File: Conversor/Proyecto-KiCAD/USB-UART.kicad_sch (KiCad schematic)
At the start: 30 parts, among them P12 USB-B, Q5 IRF7425, SW5 Switch, U14 FT232BL, U15 LP2985-3.3, Y1 6 MHz

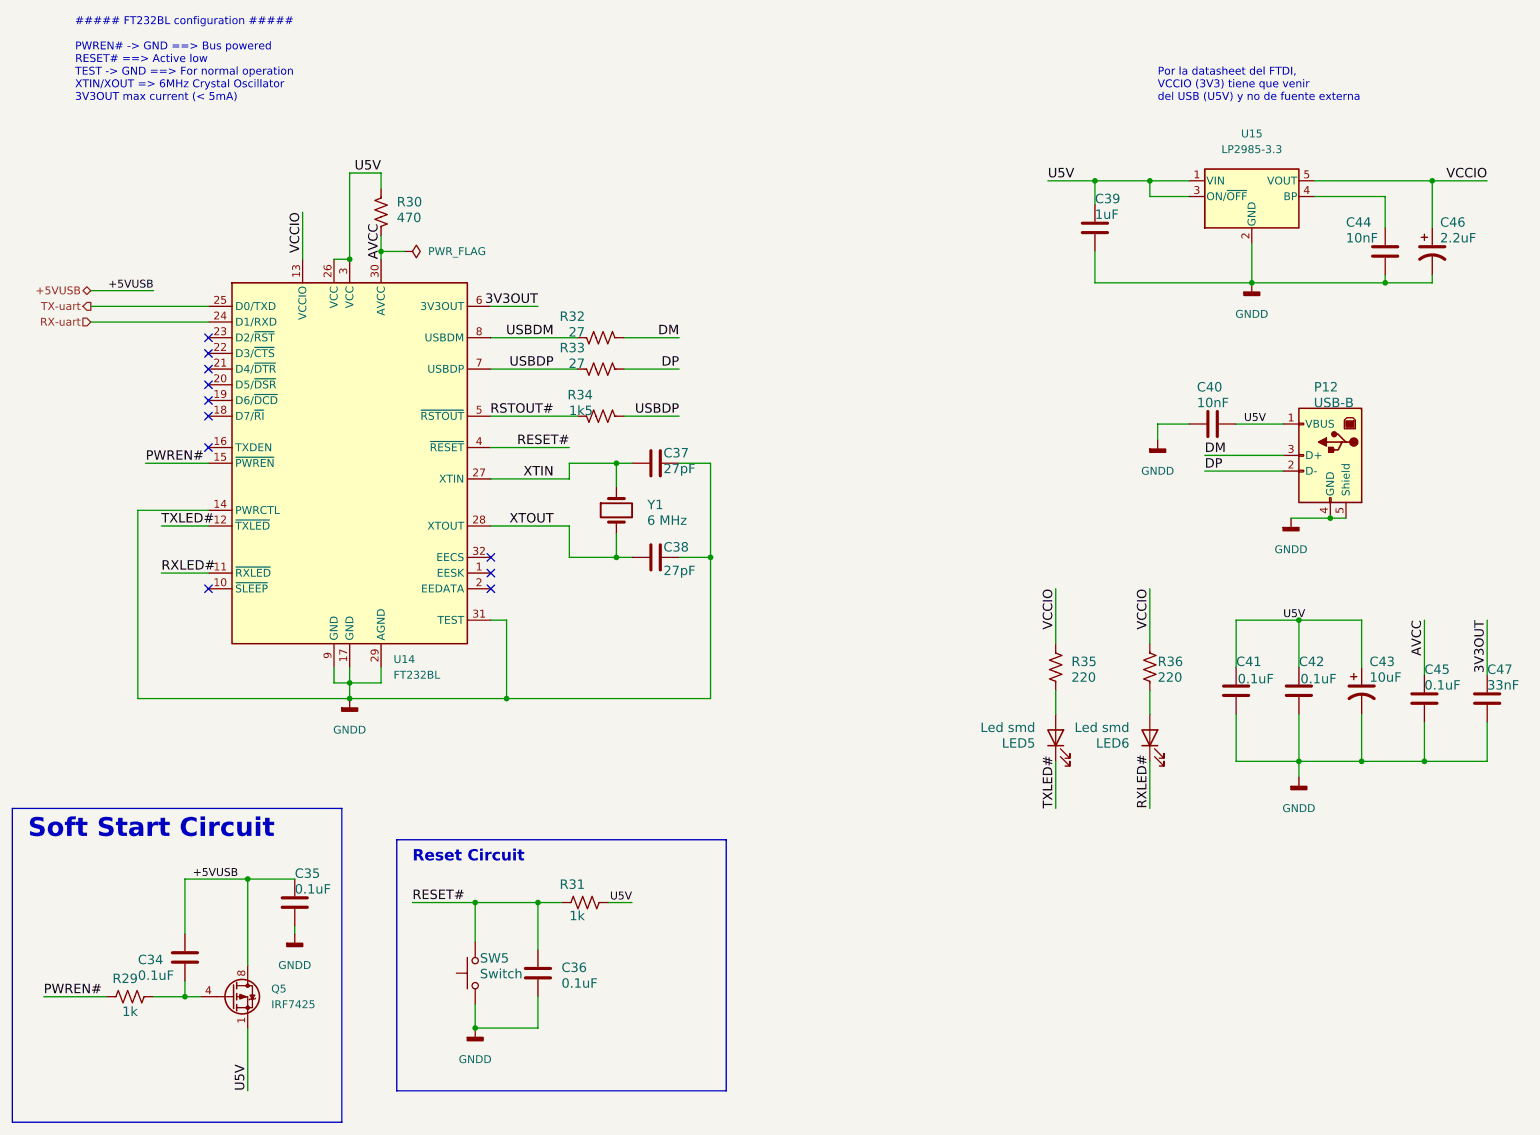
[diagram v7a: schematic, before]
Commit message: Agregar el selector de alim. de 12V y seguir emprolijando la placa
- Agregar modelos de los switches
- Agregar algunos test points
Por hacer:
  - Todo lo de los dos anteriores commits
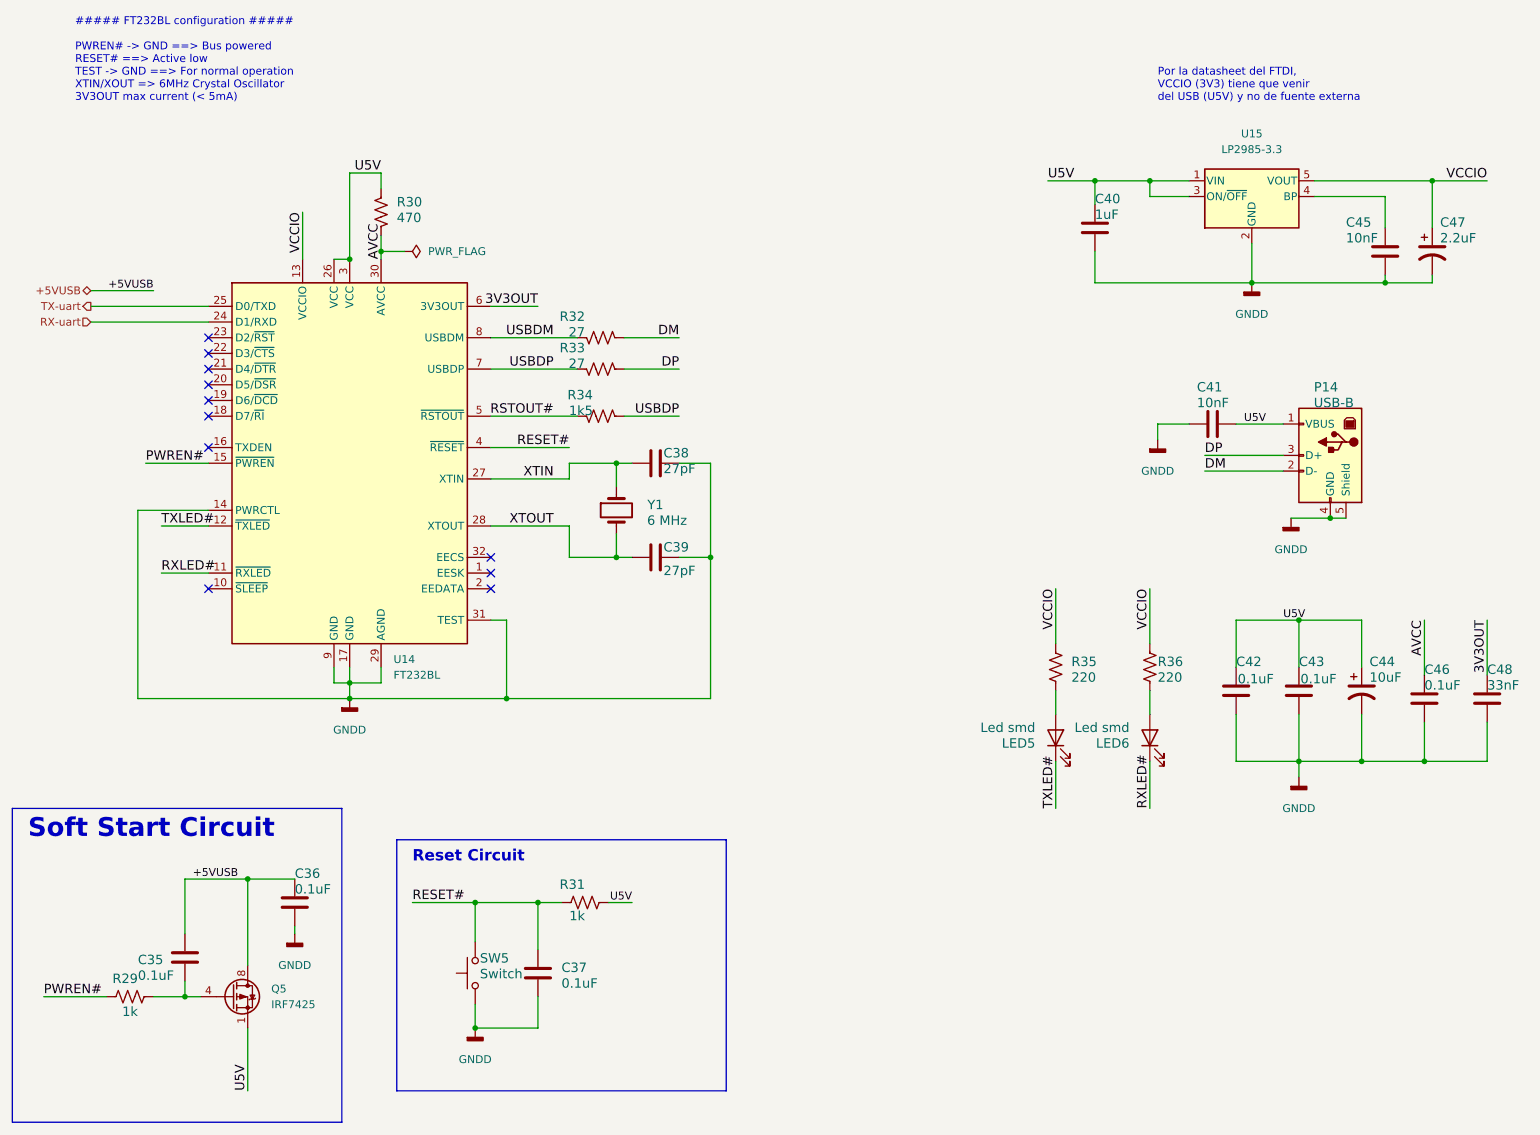
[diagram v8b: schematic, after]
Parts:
- Y1: footprint Crystal:Resonator-2Pin_W10.0mm_H5.0mm -> Crystal:Crystal_HC18-U_Vertical
- renumbered C34 to C35, C35 to C36, C36 to C37, C37 to C38, C38 to C39, C39 to C40, C40 to C41, C41 to C42, C42 to C43, C43 to C44, C44 to C45, C45 to C46, C46 to C47, C47 to C48, P12 to P14
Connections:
- net DM: now also P14.2 (D-); no longer P14.3 (D+)
- net DP: now also P14.3 (D+); no longer P14.2 (D-)
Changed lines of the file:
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@@
     (effects (font (size 1.524 1.524)) (justify left bottom))
   )
-  (label "DM" (at 212.09 86.36 0)
+  (label "DP" (at 212.09 86.36 0)
     (effects (font (size 1.524 1.524)) (justify left bottom))
   )
@@
     (effects (font (size 1.524 1.524)) (justify left bottom))
   )
-  (label "DP" (at 212.09 88.9 0)
+  (label "DM" (at 212.09 88.9 0)
     (effects (font (size 1.524 1.524)) (justify left bottom))
   )
@@
   (symbol (lib_id "Device:C") (at 123.19 87.63 90) (mirror x) (unit 1)
     (in_bom yes) (on_board yes)
-    (property "Reference" "C37" (id 0) (at 124.46 85.09 90)
+    (property "Reference" "C38" (id 0) (at 124.46 85.09 90)
       (effects (font (size 1.524 1.524)) (justify right top))
     )
@@
   (symbol (lib_id "power:GNDD") (at 226.06 96.52 0) (unit 1)
     (in_bom yes) (on_board yes) (fields_autoplaced)
-    (property "Reference" "#PWR0129" (id 0) (at 226.06 102.87 0)
+    (property "Reference" "#PWR090" (id 0) (at 226.06 102.87 0)
       (effects (font (size 1.27 1.27)) hide)
     )
@@
   (symbol (lib_id "power:GNDD") (at 204.47 83.82 0) (unit 1)
     (in_bom yes) (on_board yes) (fields_autoplaced)
-    (property "Reference" "#PWR0125" (id 0) (at 204.47 90.17 0)
+    (property "Reference" "#PWR088" (id 0) (at 204.47 90.17 0)
       (effects (font (size 1.27 1.27)) hide)
     )
@@
   (symbol (lib_id "power:GNDD") (at 219.71 58.42 0) (unit 1)
     (in_bom yes) (on_board yes) (fields_autoplaced)
-    (property "Reference" "#PWR0124" (id 0) (at 219.71 64.77 0)
+    (property "Reference" "#PWR089" (id 0) (at 219.71 64.77 0)
       (effects (font (size 1.27 1.27)) hide)
     )
@@
   (symbol (lib_id "Device:C") (at 46.99 167.64 0) (unit 1)
     (in_bom yes) (on_board yes)
-    (property "Reference" "C34" (id 0) (at 39.37 168.91 0)
+    (property "Reference" "C35" (id 0) (at 39.37 168.91 0)
       (effects (font (size 1.524 1.524)) (justify left bottom))
     )
@@
   (symbol (lib_id "Connector:USB_B") (at 232.41 86.36 0) (mirror y) (unit 1)
     (in_bom yes) (on_board yes)
-    (property "Reference" "P12" (id 0) (at 233.68 76.2 0)
+    (property "Reference" "P14" (id 0) (at 233.68 76.2 0)
       (effects (font (size 1.524 1.524)) (justify left bottom))
     )
@@
   (symbol (lib_id "power:GNDD") (at 227.33 138.43 0) (unit 1)
     (in_bom yes) (on_board yes) (fields_autoplaced)
-    (property "Reference" "#PWR0128" (id 0) (at 227.33 144.78 0)
+    (property "Reference" "#PWR091" (id 0) (at 227.33 144.78 0)
       (effects (font (size 1.27 1.27)) hide)
     )
@@
   (symbol (lib_id "power:GNDD") (at 93.98 179.07 0) (unit 1)
     (in_bom yes) (on_board yes) (fields_autoplaced)
-    (property "Reference" "#PWR0127" (id 0) (at 93.98 185.42 0)
+    (property "Reference" "#PWR087" (id 0) (at 93.98 185.42 0)
       (effects (font (size 1.27 1.27)) hide)
     )
@@
   (symbol (lib_id "Device:C") (at 257.81 125.73 180) (unit 1)
     (in_bom yes) (on_board yes)
-    (property "Reference" "C47" (id 0) (at 257.81 121.92 0)
+    (property "Reference" "C48" (id 0) (at 257.81 121.92 0)
       (effects (font (size 1.524 1.524)) (justify right top))
     )
@@
       (effects (font (size 1.524 1.524)) (justify left bottom))
     )
-    (property "Footprint" "Crystal:Resonator-2Pin_W10.0mm_H5.0mm" (id 2) (at 116.84 95.25 0)
+    (property "Footprint" "Crystal:Crystal_HC18-U_Vertical" (id 2) (at 116.84 95.25 0)
       (effects (font (size 1.27 1.27)) hide)
     )
@@
   (symbol (lib_id "power:PWR_FLAG") (at 82.55 53.34 270) (unit 1)
     (in_bom yes) (on_board yes) (fields_autoplaced)
-    (property "Reference" "#FLG0104" (id 0) (at 84.455 53.34 0)
+    (property "Reference" "#FLG05" (id 0) (at 84.455 53.34 0)
       (effects (font (size 1.27 1.27)) hide)
     )
@@
   (symbol (lib_id "power:GNDD") (at 73.66 125.73 0) (unit 1)
     (in_bom yes) (on_board yes) (fields_autoplaced)
-    (property "Reference" "#PWR0126" (id 0) (at 73.66 132.08 0)
+    (property "Reference" "#PWR086" (id 0) (at 73.66 132.08 0)
       (effects (font (size 1.27 1.27)) hide)
     )
@@
   (symbol (lib_id "Device:C") (at 194.31 49.53 0) (unit 1)
     (in_bom yes) (on_board yes)
-    (property "Reference" "C39" (id 0) (at 194.31 45.72 0)
+    (property "Reference" "C40" (id 0) (at 194.31 45.72 0)
       (effects (font (size 1.524 1.524)) (justify left bottom))
     )
@@
   (symbol (lib_id "Device:C_Polarized_US") (at 237.49 124.46 0) (unit 1)
     (in_bom yes) (on_board yes)
-    (property "Reference" "C43" (id 0) (at 238.76 120.65 0)
+    (property "Reference" "C44" (id 0) (at 238.76 120.65 0)
       (effects (font (size 1.524 1.524)) (justify left bottom))
     )
@@
   (symbol (lib_id "Device:C") (at 227.33 124.46 180) (unit 1)
     (in_bom yes) (on_board yes)
-    (property "Reference" "C42" (id 0) (at 227.33 120.65 0)
+    (property "Reference" "C43" (id 0) (at 227.33 120.65 0)
       (effects (font (size 1.524 1.524)) (justify right top))
     )
@@
   (symbol (lib_id "Device:C_Polarized_US") (at 248.92 53.34 0) (unit 1)
     (in_bom yes) (on_board yes)
-    (property "Reference" "C46" (id 0) (at 250.19 49.53 0)
+    (property "Reference" "C47" (id 0) (at 250.19 49.53 0)
       (effects (font (size 1.524 1.524)) (justify left bottom))
     )
@@
   (symbol (lib_id "Device:C") (at 217.17 124.46 180) (unit 1)
     (in_bom yes) (on_board yes)
-    (property "Reference" "C41" (id 0) (at 217.17 120.65 0)
+    (property "Reference" "C42" (id 0) (at 217.17 120.65 0)
       (effects (font (size 1.524 1.524)) (justify right top))
     )
@@
   (symbol (lib_id "power:GNDD") (at 64.77 163.83 0) (unit 1)
     (in_bom yes) (on_board yes) (fields_autoplaced)
-    (property "Reference" "#PWR0142" (id 0) (at 64.77 170.18 0)
+    (property "Reference" "#PWR085" (id 0) (at 64.77 170.18 0)
       (effects (font (size 1.27 1.27)) hide)
     )
@@
   (symbol (lib_id "Device:C") (at 241.3 53.34 0) (unit 1)
     (in_bom yes) (on_board yes)
-    (property "Reference" "C44" (id 0) (at 234.95 49.53 0)
+    (property "Reference" "C45" (id 0) (at 234.95 49.53 0)
       (effects (font (size 1.524 1.524)) (justify left bottom))
     )
@@
   (symbol (lib_id "Device:C") (at 123.19 102.87 90) (mirror x) (unit 1)
     (in_bom yes) (on_board yes)
-    (property "Reference" "C38" (id 0) (at 124.46 100.33 90)
+    (property "Reference" "C39" (id 0) (at 124.46 100.33 90)
       (effects (font (size 1.524 1.524)) (justify right top))
     )
@@
   (symbol (lib_id "Device:C") (at 104.14 170.18 0) (unit 1)
     (in_bom yes) (on_board yes)
-    (property "Reference" "C36" (id 0) (at 107.95 170.18 0)
+    (property "Reference" "C37" (id 0) (at 107.95 170.18 0)
       (effects (font (size 1.524 1.524)) (justify left bottom))
     )
@@
   (symbol (lib_id "Device:C") (at 64.77 158.75 0) (unit 1)
     (in_bom yes) (on_board yes)
-    (property "Reference" "C35" (id 0) (at 64.77 154.94 0)
+    (property "Reference" "C36" (id 0) (at 64.77 154.94 0)
       (effects (font (size 1.524 1.524)) (justify left bottom))
     )
@@
   (symbol (lib_id "Device:C") (at 247.65 125.73 180) (unit 1)
     (in_bom yes) (on_board yes)
-    (property "Reference" "C45" (id 0) (at 247.65 121.92 0)
+    (property "Reference" "C46" (id 0) (at 247.65 121.92 0)
       (effects (font (size 1.524 1.524)) (justify right top))
     )
@@
   (symbol (lib_id "Device:C") (at 213.36 81.28 90) (unit 1)
     (in_bom yes) (on_board yes)
-    (property "Reference" "C40" (id 0) (at 210.82 76.2 90)
-      (effects (font (size 1.524 1.524)) (justify right top))
-    )
+    (property "Reference" "C41" (id 0) (at 210.82 76.2 90)
+      (effects (font (size 1.524 1.524)) (justify right top))
+    )
